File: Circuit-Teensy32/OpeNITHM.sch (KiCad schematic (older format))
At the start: 25 parts, among them J1 Conn_01x14, J2 Conn_01x14, J7 Conn_02x12_Odd_Even, J8 Conn_02x12_Odd_Even, J9 Conn_01x05, U1 74HC4051, U2 74HC4051, U3 74HC4051, U4 74HC4051

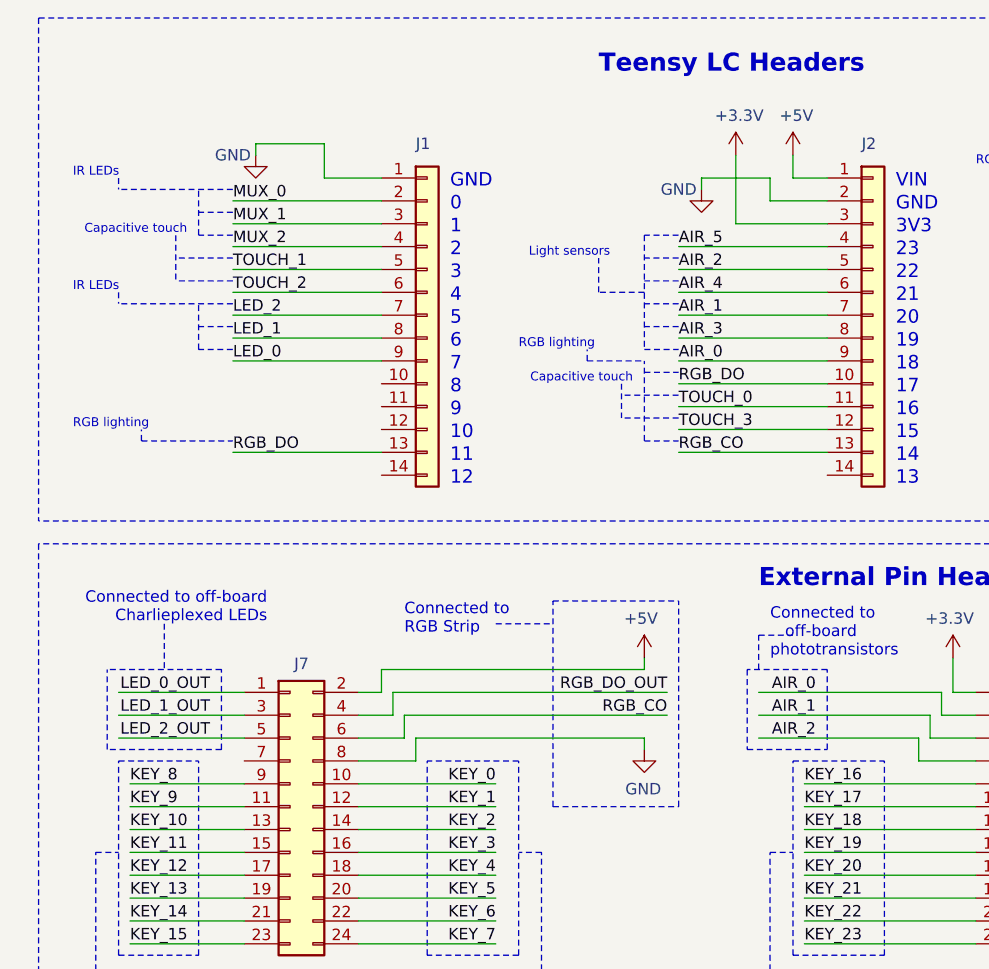
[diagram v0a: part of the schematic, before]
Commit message: Update 32 key board to v2.1
Reorganizes pins so DMA can be used, drops APA102 support, adds additional pins for complex IR LED boards.
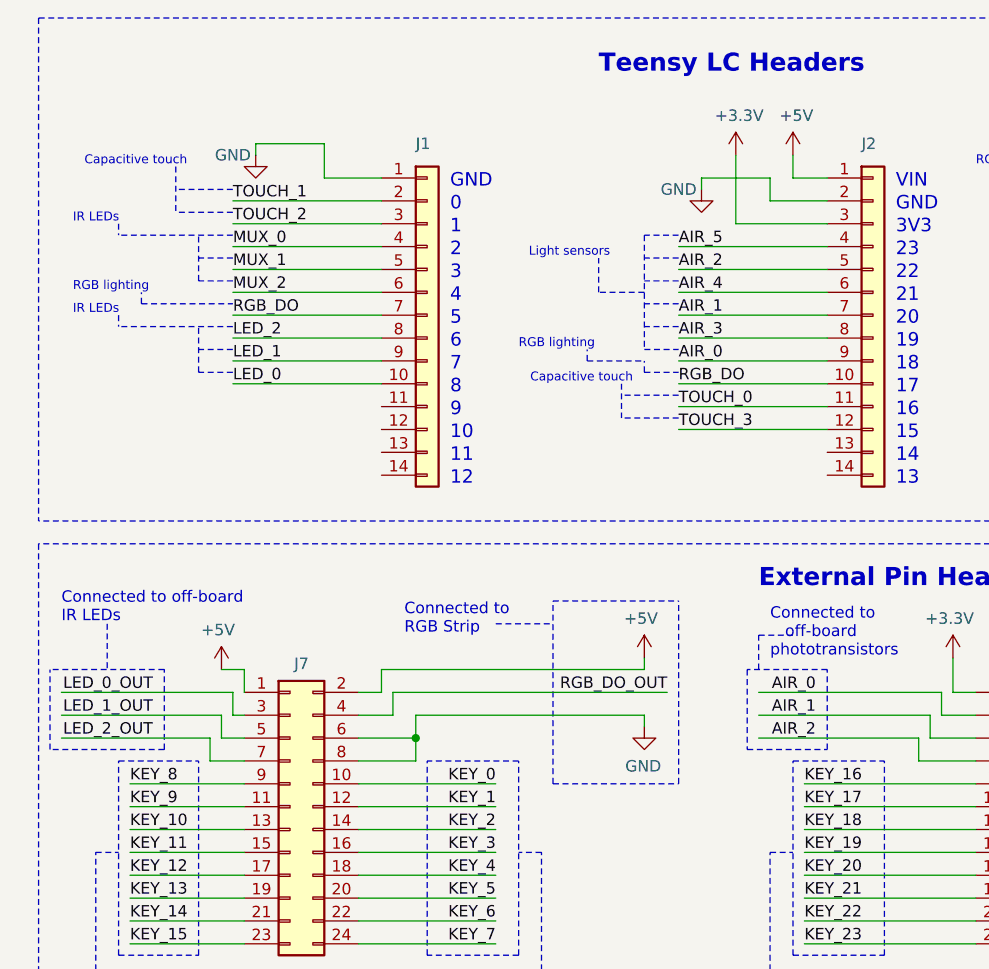
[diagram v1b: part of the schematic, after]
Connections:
- net labels removed: RGB_CO
- wire segments 245 -> 251
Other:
- note added: "Connected to off-board \nIR LEDs"
- note removed: "Connected to off-board\nCharlieplexed LEDs"
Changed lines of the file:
@@
 Title "OpeNITHM Controller Board"
 Date "2020-06-03"
-Rev "v2.0"
+Rev "v2.1"
 Comp ""
 Comment1 ""
@@
 Text Label 1050 4700 0    50   ~ 0
 KEY_15
-Text Label 1400 3600 2    50   ~ 0
+Text Label 1150 3600 2    50   ~ 0
 LED_0_OUT
-Text Label 1400 3700 2    50   ~ 0
+Text Label 1150 3700 2    50   ~ 0
 LED_1_OUT
-Text Label 1400 3800 2    50   ~ 0
+Text Label 1150 3800 2    50   ~ 0
 LED_2_OUT
 Wire Wire Line
 	3300 3500 3300 3450
 Wire Wire Line
-	3300 3800 3300 3850
-Text Label 3400 3700 2    50   ~ 0
-RGB_CO
+	3300 3700 3300 3750
 Text Label 3400 3600 2    50   ~ 0
 RGB_DO_OUT
@@
 L power:GND #PWR0112
 U 1 1 5D492DBE
-P 3300 3850
-F 0 "#PWR0112" H 3300 3600 50  0001 C CNN
-F 1 "GND" H 3305 3677 50  0000 C CNN
-F 2 "" H 3300 3850 50  0001 C CNN
-F 3 "" H 3300 3850 50  0001 C CNN
-	1    3300 3850
+P 3300 3750
+F 0 "#PWR0112" H 3300 3500 50  0001 C CNN
+F 1 "GND" H 3305 3577 50  0000 C CNN
+F 2 "" H 3300 3750 50  0001 C CNN
+F 3 "" H 3300 3750 50  0001 C CNN
+	1    3300 3750
 	-1   0    0    -1
 $EndComp
@@
 $EndComp
 Wire Wire Line
-	1000 3600 1550 3600
-Wire Wire Line
-	1000 3800 1550 3800
-Wire Wire Line
-	1000 3700 1550 3700
-Wire Wire Line
-	2150 2050 1500 2050
-Text Label 1500 2050 0    50   ~ 0
+	2150 2150 1500 2150
+Text Label 1500 2150 0    50   ~ 0
 LED_1
-Text Label 1500 1650 0    50   ~ 0
+Text Label 1500 1850 0    50   ~ 0
 MUX_2
 Wire Wire Line
-	2150 1550 1500 1550
-Wire Wire Line
-	1500 1650 2150 1650
+	2150 1750 1500 1750
+Wire Wire Line
+	1500 1850 2150 1850
 Text Notes 4400 2700 0    59   ~ 0
 13
-Text Label 3450 2550 0    50   ~ 0
-RGB_CO
-Wire Wire Line
-	3450 2550 4100 2550
 Wire Wire Line
 	3450 2150 4100 2150
@@
 	1900 6350 1900 6800
 Wire Notes Line
-	1500 1700 1250 1700
-Text Notes 1300 1600 2    39   ~ 0
+	1500 1400 1250 1400
+Text Notes 1300 1300 2    39   ~ 0
 Capacitive touch
 Text Label 8000 4850 0    50   ~ 0
@@
 	7150 5950 7800 5950
 Wire Wire Line
-	2150 1750 1500 1750
-Text Label 1500 1750 0    50   ~ 0
+	2150 1450 1500 1450
+Text Label 1500 1450 0    50   ~ 0
 TOUCH_1
 Wire Notes Line rgb(181, 36, 0)
-	1500 1900 1000 1900
+	1500 2000 1000 2000
 Wire Notes Line rgb(181, 36, 0)
-	1000 1850 1000 1900
-Text Notes 800  1850 0    39   ~ 0
+	1000 1950 1000 2000
+Text Notes 800  1950 0    39   ~ 0
 IR LEDs
 Wire Notes Line rgb(181, 36, 0)
-	1500 2100 1350 2100
+	1500 2200 1350 2200
 Wire Notes Line rgb(181, 36, 0)
-	1350 2100 1350 1900
+	1350 2200 1350 2000
 Wire Notes Line rgb(99, 255, 8)
 	5050 1350 5050 1300
@@
 	6450 2950 6450 5200
 Wire Notes Line
-	1450 3500 950  3500
-Text Notes 1650 3300 2    50   ~ 0
-Connected to off-board\nCharlieplexed LEDs
-Wire Notes Line
-	1200 3300 1200 3500
+	1200 3500 700  3500
+Text Notes 750  3300 0    50   ~ 0
+Connected to off-board \nIR LEDs
+Wire Notes Line
+	950  3300 950  3500
 Wire Notes Line
 	6600 5750 6600 6450
@@
 	11050 5750 11050 6450
 Wire Notes Line
-	2900 4100 3450 4100
-Wire Notes Line
-	2900 4100 2900 3200
-Wire Notes Line
-	3450 4100 3450 3200
+	2900 4000 3450 4000
+Wire Notes Line
+	2900 4000 2900 3200
+Wire Notes Line
+	3450 4000 3450 3200
 Wire Notes Line
 	2900 3200 3450 3200
@@
 	3450 2000 3300 2000
 Wire Notes Line rgb(181, 36, 0)
-	1500 2000 1350 2000
+	1500 2100 1350 2100
 Wire Notes Line rgb(255, 153, 9)
-	1500 1400 1000 1400
+	1500 1600 1000 1600
 Wire Notes Line rgb(255, 153, 90)
-	1000 1350 1000 1400
-Text Notes 800  1350 0    39   ~ 0
+	1000 1550 1000 1600
+Text Notes 800  1550 0    39   ~ 0
 IR LEDs
 Wire Notes Line rgb(255, 153, 9)
-	1500 1600 1350 1600
+	1500 1800 1350 1800
 Wire Notes Line rgb(255, 153, 9)
-	1350 1600 1350 1400
+	1350 1800 1350 1600
 Wire Notes Line rgb(255, 153, 9)
-	1500 1500 1350 1500
-Wire Wire Line
-	1500 1450 2150 1450
-Text Label 1500 1550 0    50   ~ 0
+	1500 1700 1350 1700
+Wire Wire Line
+	1500 1650 2150 1650
+Text Label 1500 1750 0    50   ~ 0
 MUX_1
-Text Label 1500 1450 0    50   ~ 0
+Text Label 1500 1650 0    50   ~ 0
 MUX_0
 Text Notes 3250 2250 2    39   ~ 0
@@
 	5650 3300 5650 3350
 Wire Notes Line
-	1250 1600 1250 1800
+	1250 1300 1250 1500
 Text Label 8450 3550 2    50   ~ 0
 KEY_24
@@
 	10250 1450 10750 1450
 Wire Wire Line
-	2150 1850 1500 1850
-Text Label 1500 1850 0    50   ~ 0
+	2150 1550 1500 1550
+Text Label 1500 1550 0    50   ~ 0
 TOUCH_2
 Text Label 3450 2450 0    50   ~ 0
@@
 	3450 2450 4100 2450
 Wire Notes Line
-	1500 1800 1250 1800
+	1500 1500 1250 1500
 Wire Notes Line
 	3200 2250 3200 2400
@@
 	3450 2300 3200 2300
 Wire Notes Line rgb(90, 238, 7)
-	3300 2500 3450 2500
-Wire Notes Line rgb(90, 238, 7)
 	3300 2200 3450 2200
-Wire Notes Line rgb(90, 238, 7)
-	3300 2500 3300 2150
 Wire Notes Line rgb(90, 238, 7)
 	3050 2150 3050 2100
@@
 $EndComp
 Wire Notes Line
-	950  3850 950  3500
-Wire Notes Line
-	1450 3850 1450 3500
-Wire Notes Line
-	1450 3850 950  3850
+	700  3850 700  3500
+Wire Notes Line
+	1200 3850 1200 3500
+Wire Notes Line
+	1200 3850 700  3850
 Text Label 2650 4000 2    50   ~ 0
 KEY_0
@@
 	2300 3900 2300 3800
 Wire Wire Line
-	2300 3800 3300 3800
+	2300 3700 3300 3700
 Wire Notes Line
 	2850 4300 2750 4300
 Wire Wire Line
-	2250 3800 2250 3700
-Wire Wire Line
-	2250 3700 3400 3700
-Wire Wire Line
 	2200 3700 2200 3600
 Wire Wire Line
@@
 Wire Wire Line
 	2050 3700 2200 3700
-Wire Wire Line
-	2050 3800 2250 3800
 Wire Wire Line
 	2050 3900 2300 3900
@@
 	0    1    1    0
 $EndComp
-Text Label 1500 1950 0    50   ~ 0
+Text Label 1500 2050 0    50   ~ 0
 LED_2
 Wire Wire Line
-	1500 1950 2150 1950
+	1500 2050 2150 2050
 Wire Wire Line
 	8050 2150 8550 2150
 Text Label 8400 2150 2    50   ~ 0
 KEY_8
-Text Label 1500 2150 0    50   ~ 0
+Text Label 1500 2250 0    50   ~ 0
 LED_0
 Wire Wire Line
-	1500 2150 2150 2150
+	1500 2250 2150 2250
 Wire Notes Line rgb(90, 238, 7)
-	1100 2500 1100 2450
-Text Notes 800  2450 0    39   ~ 0
+	1100 1900 1100 1850
+Text Notes 800  1850 0    39   ~ 0
 RGB lighting
 Wire Notes Line rgb(90, 238, 7)
-	1100 2500 1500 2500
-Wire Wire Line
-	1500 2550 2150 2550
-Text Label 1500 2550 0    50   ~ 0
+	1100 1900 1500 1900
+Wire Wire Line
+	1500 1950 2150 1950
+Text Label 1500 1950 0    50   ~ 0
 RGB_DO
 $Comp
@@
 Text Notes 4500 6650 0    50   ~ 0
 NOTE:\nR_AIR is highly dependent on your \nIR leds and phototransistor/diodes.\nThey may range from \n10k Ohm to 2M Ohm.
+Wire Wire Line
+	2050 3800 2300 3800
+$Comp
+L power:+5V #PWR0121
+U 1 1 5F2974C6
+P 1450 3500
+F 0 "#PWR0121" H 1450 3350 50  0001 C CNN
+F 1 "+5V" H 1465 3673 50  0000 C CNN
+F 2 "" H 1450 3500 50  0001 C CNN
+F 3 "" H 1450 3500 50  0001 C CNN
+	1    1450 3500
+	-1   0    0    -1
+$EndComp
+Wire Wire Line
+	2300 3800 2300 3700
+Connection ~ 2300 3800
+Wire Notes Line rgb(90, 238, 7)
+	3300 2200 3300 2150
+Wire Wire Line
+	1550 3900 1400 3900
+Wire Wire Line
+	1400 3900 1400 3800
+Wire Wire Line
+	750  3800 1400 3800
+Wire Wire Line
+	1550 3800 1450 3800
+Wire Wire Line
+	1450 3800 1450 3700
+Wire Wire Line
+	750  3700 1450 3700
+Wire Wire Line
+	1550 3700 1500 3700
+Wire Wire Line
+	1500 3700 1500 3600
+Wire Wire Line
+	750  3600 1500 3600
+Wire Wire Line
+	1550 3600 1550 3500
+Wire Wire Line
+	1550 3500 1450 3500
 $EndSCHEMATC

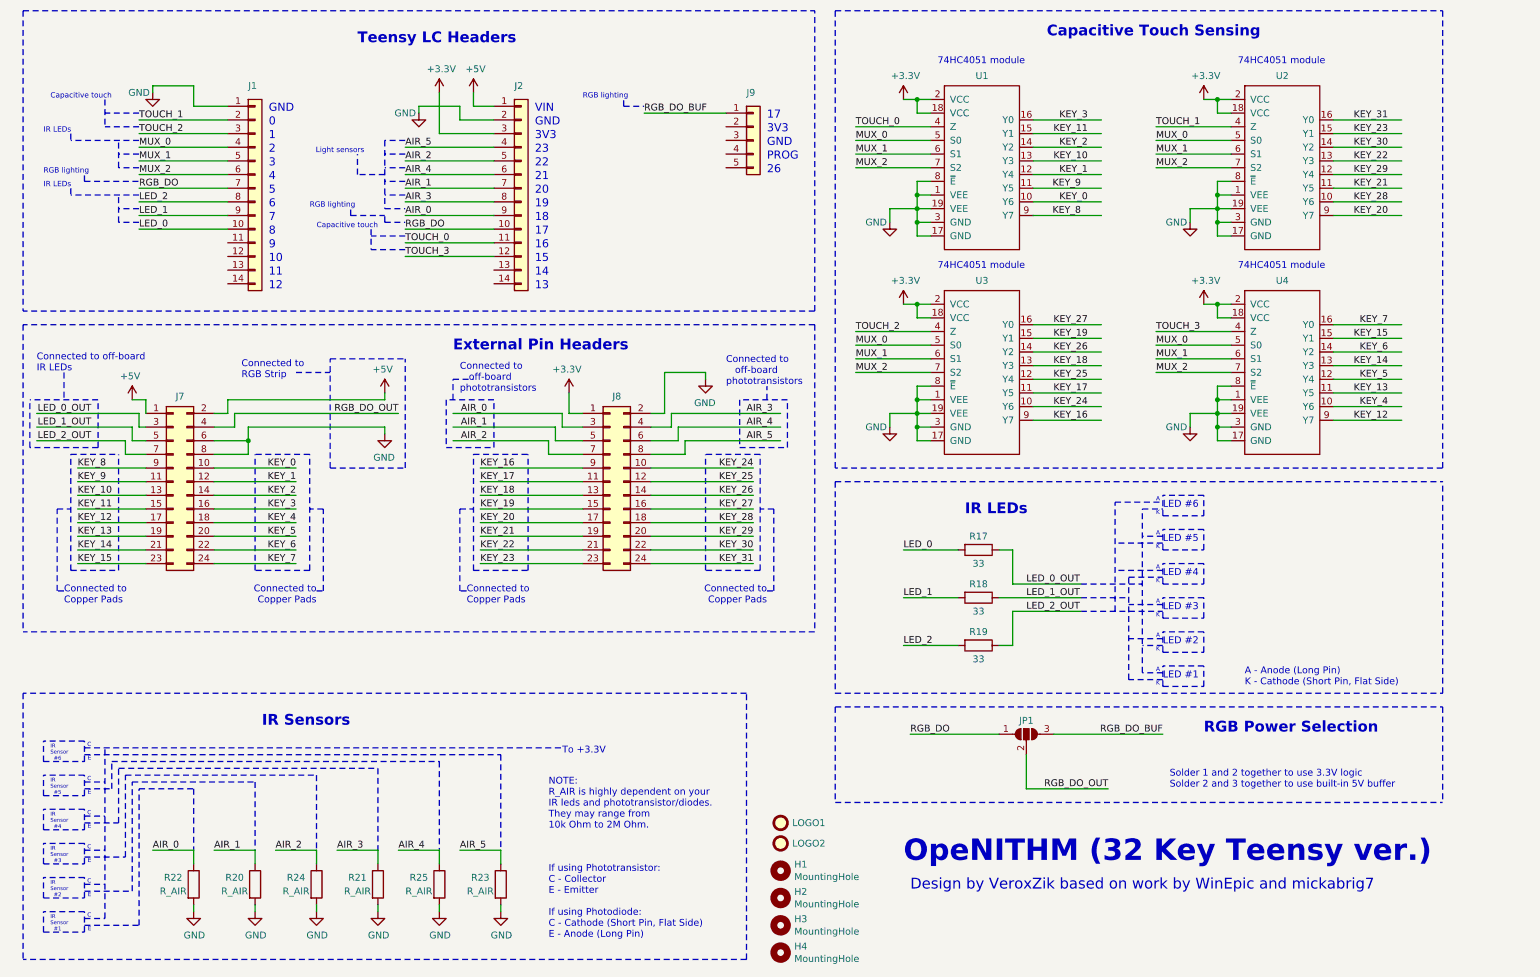
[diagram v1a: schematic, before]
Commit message: Changes to v2.1
Broke out all spare pins to Teensy,
No more solder jumper for RGB data line,
Added solder jumper for IR LED power option (+5v by default)
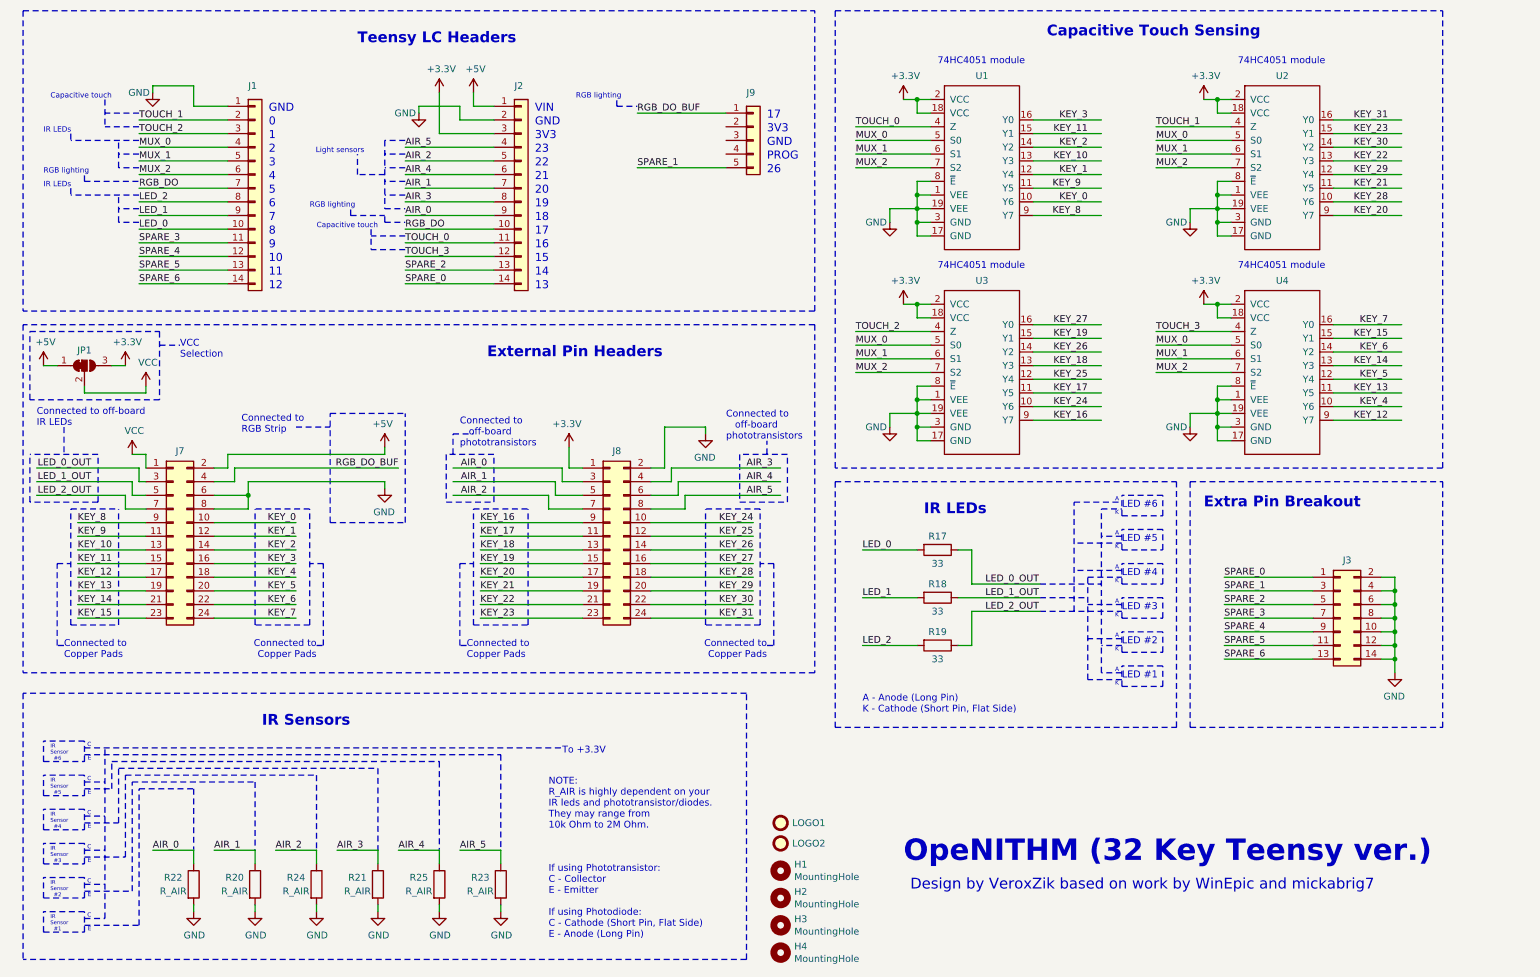
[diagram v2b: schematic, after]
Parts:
- removed JP1: SolderJumper_3_Open, Jumper:SolderJumper-3_P1.3mm_Open_RoundedPad1.0x1.5mm, symbol Jumper:SolderJumper_3_Open
- added J3: Conn_02x07_Odd_Even, Connector_PinHeader_2.54mm:PinHeader_2x07_P2.54mm_Horizontal, symbol Connector_Generic:Conn_02x07_Odd_Even
- added JP1: SolderJumper_3_Bridged12, Jumper:SolderJumper-3_P1.3mm_Bridged12_RoundedPad1.0x1.5mm, symbol Jumper:SolderJumper_3_Bridged12
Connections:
- net labels added: SPARE_0, SPARE_1, SPARE_2, SPARE_3, SPARE_4, SPARE_5, SPARE_6, VCC
- net labels removed: RGB_DO_OUT
- wire segments 251 -> 280
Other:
- note added: "Extra Pin Breakout"
- note added: "VCC\nSelection"
- note removed: "RGB Power Selection"
- note removed: "Solder 1 and 2 together to use 3.3V logic\nSolder 2 and 3 together to use built-in 5V buffer"
- moved on the sheet: J7, J8, R17, R18, R19
